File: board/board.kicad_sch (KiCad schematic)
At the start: 17 parts, among them J1 Conn_01x10_Pin, J2 Conn_01x10, U1 nPM1300-CAXX

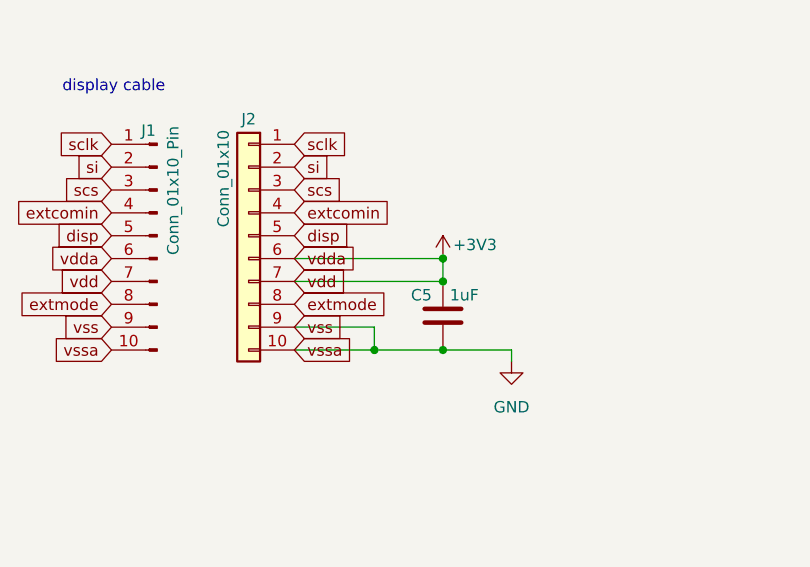
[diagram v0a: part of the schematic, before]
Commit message: board: sch display add extmode and extcomin
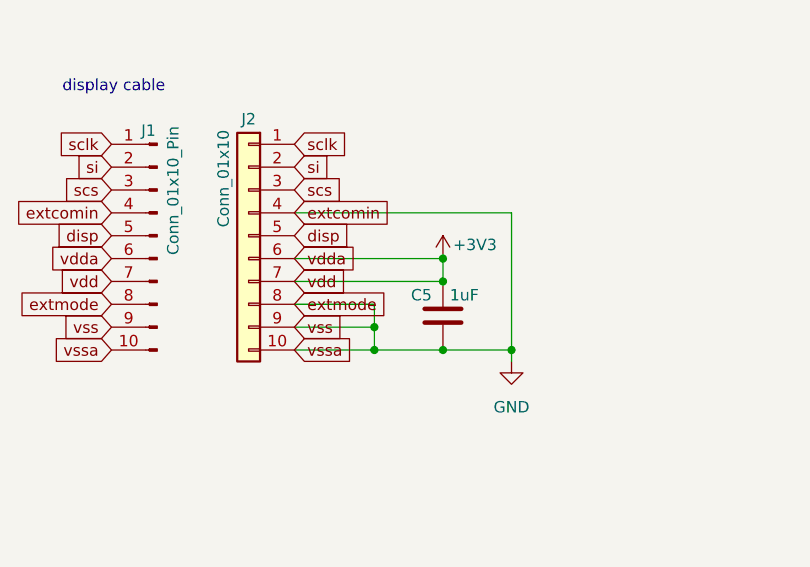
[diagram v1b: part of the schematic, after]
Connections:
- net extcomin is gone; now on net GND: J1.4 (Pin_4), J2.4 (Pin_4)
- net extmode is gone; now on net GND: J1.8 (Pin_8), J2.8 (Pin_8)
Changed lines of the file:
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@@
+	)
+	(junction
+		(at 54.61 48.26)
+		(diameter 0)
+		(color 0 0 0 0)
 	)
 	(junction
@@
 	)
 	(junction
+		(at 69.85 50.8)
+		(diameter 0)
+		(color 0 0 0 0)
+	)
+	(junction
 		(at 261.62 41.91)
 		(diameter 0)
@@
 	(wire
 		(pts
+			(xy 45.72 45.72) (xy 54.61 45.72)
+		)
+		(stroke
+			(width 0)
+			(type default)
+		)
+	)
+	(wire
+		(pts
 			(xy 254 60.96) (xy 252.73 60.96)
 		)
@@
 	(wire
 		(pts
+			(xy 54.61 45.72) (xy 54.61 48.26)
+		)
+		(stroke
+			(width 0)
+			(type default)
+		)
+	)
+	(wire
+		(pts
 			(xy 215.9 20.32) (xy 218.44 20.32)
 		)
@@
 	(wire
 		(pts
+			(xy 69.85 35.56) (xy 69.85 50.8)
+		)
+		(stroke
+			(width 0)
+			(type default)
+		)
+	)
+	(wire
+		(pts
 			(xy 215.9 102.87) (xy 215.9 104.14)
 		)
@@
 		)
 		(stroke
+			(width 0)
+			(type default)
+		)
+	)
+	(wire
+		(pts
+			(xy 45.72 35.56) (xy 69.85 35.56)
+		)
+		(stroke

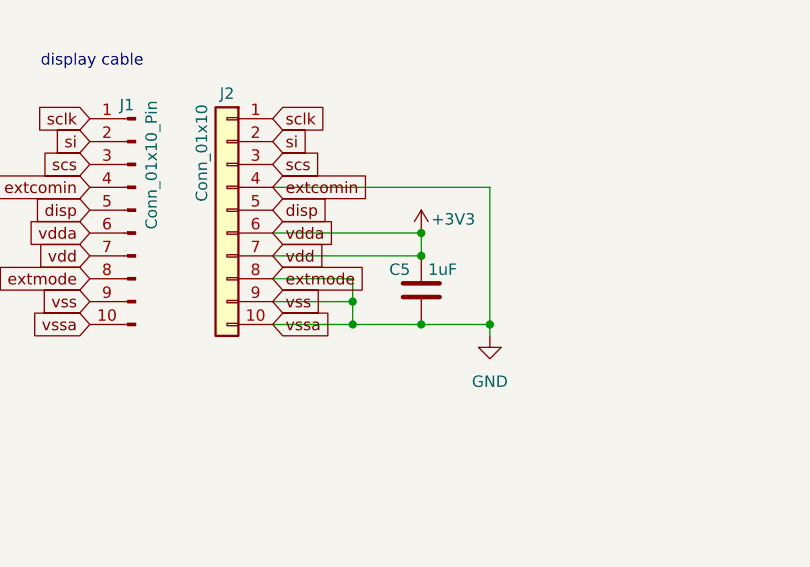
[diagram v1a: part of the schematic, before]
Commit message: board: sch display add disp signal
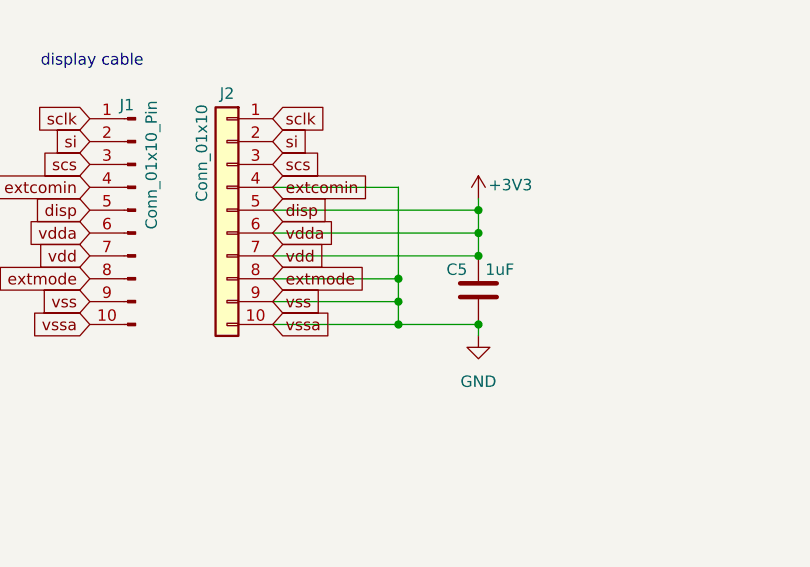
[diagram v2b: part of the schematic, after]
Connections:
- net disp is gone; now on net +3V3: J1.5 (Pin_5), J2.5 (Pin_5)
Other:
- moved on the sheet: C5
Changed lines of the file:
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@@
-	)
-	(junction
-		(at 54.61 48.26)
-		(diameter 0)
-		(color 0 0 0 0)
 	)
 	(junction
@@
 	)
 	(junction
-		(at 62.23 50.8)
+		(at 68.58 50.8)
 		(diameter 0)
 		(color 0 0 0 0)
@@
 	)
 	(junction
-		(at 62.23 40.64)
+		(at 68.58 38.1)
 		(diameter 0)
 		(color 0 0 0 0)
 	)
 	(junction
-		(at 54.61 50.8)
+		(at 59.69 50.8)
+		(diameter 0)
+		(color 0 0 0 0)
+	)
+	(junction
+		(at 68.58 40.64)
 		(diameter 0)
 		(color 0 0 0 0)
@@
 	)
 	(junction
-		(at 69.85 50.8)
+		(at 59.69 45.72)
+		(diameter 0)
+		(color 0 0 0 0)
+	)
+	(junction
+		(at 59.69 48.26)
 		(diameter 0)
 		(color 0 0 0 0)
@@
 	)
 	(junction
-		(at 62.23 43.18)
+		(at 68.58 43.18)
 		(diameter 0)
 		(color 0 0 0 0)
@@
 	(wire
 		(pts
-			(xy 54.61 48.26) (xy 54.61 50.8)
+			(xy 59.69 48.26) (xy 59.69 50.8)
 		)
 		(stroke
@@
 	(wire
 		(pts
-			(xy 54.61 50.8) (xy 62.23 50.8)
-		)
-		(stroke
-			(width 0)
-			(type default)
-		)
-	)
-	(wire
-		(pts
-			(xy 45.72 48.26) (xy 54.61 48.26)
-		)
-		(stroke
-			(width 0)
-			(type default)
-		)
-	)
-	(wire
-		(pts
-			(xy 62.23 40.64) (xy 62.23 43.18)
-		)
-		(stroke
-			(width 0)
-			(type default)
-		)
-	)
-	(wire
-		(pts
-			(xy 45.72 45.72) (xy 54.61 45.72)
+			(xy 45.72 48.26) (xy 59.69 48.26)
+		)
+		(stroke
+			(width 0)
+			(type default)
+		)
+	)
+	(wire
+		(pts
+			(xy 68.58 40.64) (xy 68.58 43.18)
+		)
+		(stroke
+			(width 0)
+			(type default)
+		)
+	)
+	(wire
+		(pts
+			(xy 45.72 45.72) (xy 59.69 45.72)
 		)
 		(stroke
@@
 	(wire
 		(pts
+			(xy 59.69 50.8) (xy 68.58 50.8)
+		)
+		(stroke
+			(width 0)
+			(type default)
+		)
+	)
+	(wire
+		(pts
 			(xy 252.73 57.15) (xy 266.7 57.15)
 		)
@@
 	(wire
 		(pts
-			(xy 45.72 43.18) (xy 62.23 43.18)
-		)
-		(stroke
-			(width 0)
-			(type default)
-		)
-	)
-	(wire
-		(pts
-			(xy 54.61 45.72) (xy 54.61 48.26)
+			(xy 59.69 45.72) (xy 59.69 48.26)
 		)
 		(stroke
@@
 	(wire
 		(pts
-			(xy 69.85 52.07) (xy 69.85 50.8)
-		)
-		(stroke
-			(width 0)
-			(type default)
-		)
-	)
-	(wire
-		(pts
-			(xy 69.85 35.56) (xy 69.85 50.8)
+			(xy 68.58 52.07) (xy 68.58 50.8)
+		)
+		(stroke
+			(width 0)
+			(type default)
+		)
+	)
+	(wire
+		(pts
+			(xy 59.69 35.56) (xy 59.69 45.72)
 		)
 		(stroke
@@
 	(wire
 		(pts
+			(xy 45.72 38.1) (xy 68.58 38.1)
+		)
+		(stroke
+			(width 0)
+			(type default)
+		)
+	)
+	(wire
+		(pts
+			(xy 45.72 43.18) (xy 68.58 43.18)
+		)
+		(stroke
+			(width 0)
+			(type default)
+		)
+	)
+	(wire
+		(pts
 			(xy 173.99 74.93) (xy 180.34 74.93)
 		)
@@
 	(wire
 		(pts
-			(xy 45.72 40.64) (xy 62.23 40.64)
-		)
-		(stroke
-			(width 0)
-			(type default)
-		)
-	)
-	(wire
-		(pts
 			(xy 251.46 62.23) (xy 261.62 62.23)
 		)
@@
 	(wire
 		(pts
-			(xy 45.72 35.56) (xy 69.85 35.56)
-		)
-		(stroke
-			(width 0)
-			(type default)
-		)
-	)
-	(wire
-		(pts
-			(xy 69.85 50.8) (xy 62.23 50.8)
+			(xy 45.72 40.64) (xy 68.58 40.64)
 		)
 		(stroke
@@
 	(wire
 		(pts
+			(xy 68.58 38.1) (xy 68.58 40.64)
+		)
+		(stroke
+			(width 0)
+			(type default)
+		)
+	)
+	(wire
+		(pts
 			(xy 266.7 55.88) (xy 266.7 57.15)
 		)
@@
 	(wire
 		(pts
-			(xy 45.72 50.8) (xy 54.61 50.8)
+			(xy 45.72 50.8) (xy 59.69 50.8)
 		)
 		(stroke
@@
 	(wire
 		(pts
+			(xy 68.58 36.83) (xy 68.58 38.1)
+		)
+		(stroke
+			(width 0)
+			(type default)
+		)
+	)
+	(wire
+		(pts
 			(xy 252.73 41.91) (xy 255.27 41.91)
+		)
+		(stroke
+			(width 0)
+			(type default)
+		)
+	)
+	(wire
+		(pts
+			(xy 45.72 35.56) (xy 59.69 35.56)
 		)
 		(stroke
@@
 	(symbol
 		(lib_id "power:GND")
-		(at 69.85 52.07 0)
+		(at 68.58 52.07 0)
 		(unit 1)
 		(exclude_from_sim no)
@@
 		(fields_autoplaced yes)
 		(property "Reference" "#PWR012"
-			(at 69.85 58.42 0)
+			(at 68.58 58.42 0)
 			(effects
 				(font
@@
 		)
 		(property "Value" "GND"
-			(at 69.85 57.15 0)
+			(at 68.58 57.15 0)
 			(effects
 				(font
@@
 		)
 		(property "Footprint" ""
-			(at 69.85 52.07 0)
+			(at 68.58 52.07 0)
 			(effects
 				(font
@@
 		)
 		(property "Datasheet" ""
-			(at 69.85 52.07 0)
+			(at 68.58 52.07 0)
 			(effects
 				(font
@@
 		)
 		(property "Description" "Power symbol creates a global label with name \"GND\" , ground"
-			(at 69.85 52.07 0)
+			(at 68.58 52.07 0)
 			(effects
 				(font
@@
 	(symbol
 		(lib_id "power:+3V3")
-		(at 62.23 40.64 0)
+		(at 68.58 36.83 0)
 		(unit 1)
 		(exclude_from_sim no)
@@
 		(dnp no)
 		(property "Reference" "#PWR013"
-			(at 62.23 44.45 0)
+			(at 68.58 40.64 0)
 			(effects
 				(font
@@
 		)
 		(property "Value" "+3V3"
-			(at 65.786 39.116 0)
+			(at 72.136 35.306 0)
 			(effects
 				(font
@@
 		)
 		(property "Footprint" ""
-			(at 62.23 40.64 0)
+			(at 68.58 36.83 0)
 			(effects
 				(font
@@
 		)
 		(property "Datasheet" ""
-			(at 62.23 40.64 0)
+			(at 68.58 36.83 0)
 			(effects
 				(font
@@
 		)
 		(property "Description" "Power symbol creates a global label with name \"+3V3\""
-			(at 62.23 40.64 0)
+			(at 68.58 36.83 0)
 			(effects
 				(font
@@
 	(symbol
 		(lib_id "Device:C")
-		(at 62.23 46.99 0)
+		(at 68.58 46.99 0)
 		(unit 1)
 		(exclude_from_sim no)
@@
 		(dnp no)
 		(property "Reference" "C5"
-			(at 58.674 44.704 0)
+			(at 65.024 44.704 0)
 			(effects
 				(font
@@
 		)
 		(property "Value" "1uF"
-			(at 62.992 44.704 0)
+			(at 69.342 44.704 0)
 			(effects
 				(font
@@
 		)
 		(property "Footprint" ""
-			(at 63.1952 50.8 0)
+			(at 69.5452 50.8 0)
 			(effects
 				(font
@@
 		)
 		(property "Datasheet" "~"
-			(at 62.23 46.99 0)
+			(at 68.58 46.99 0)
 			(effects
 				(font
@@
 		)
 		(property "Description" "Unpolarized capacitor"
-			(at 62.23 46.99 0)
-			(effects
-				(font
+			(at 68.58 46.99 0)
+			(effects
+				(font

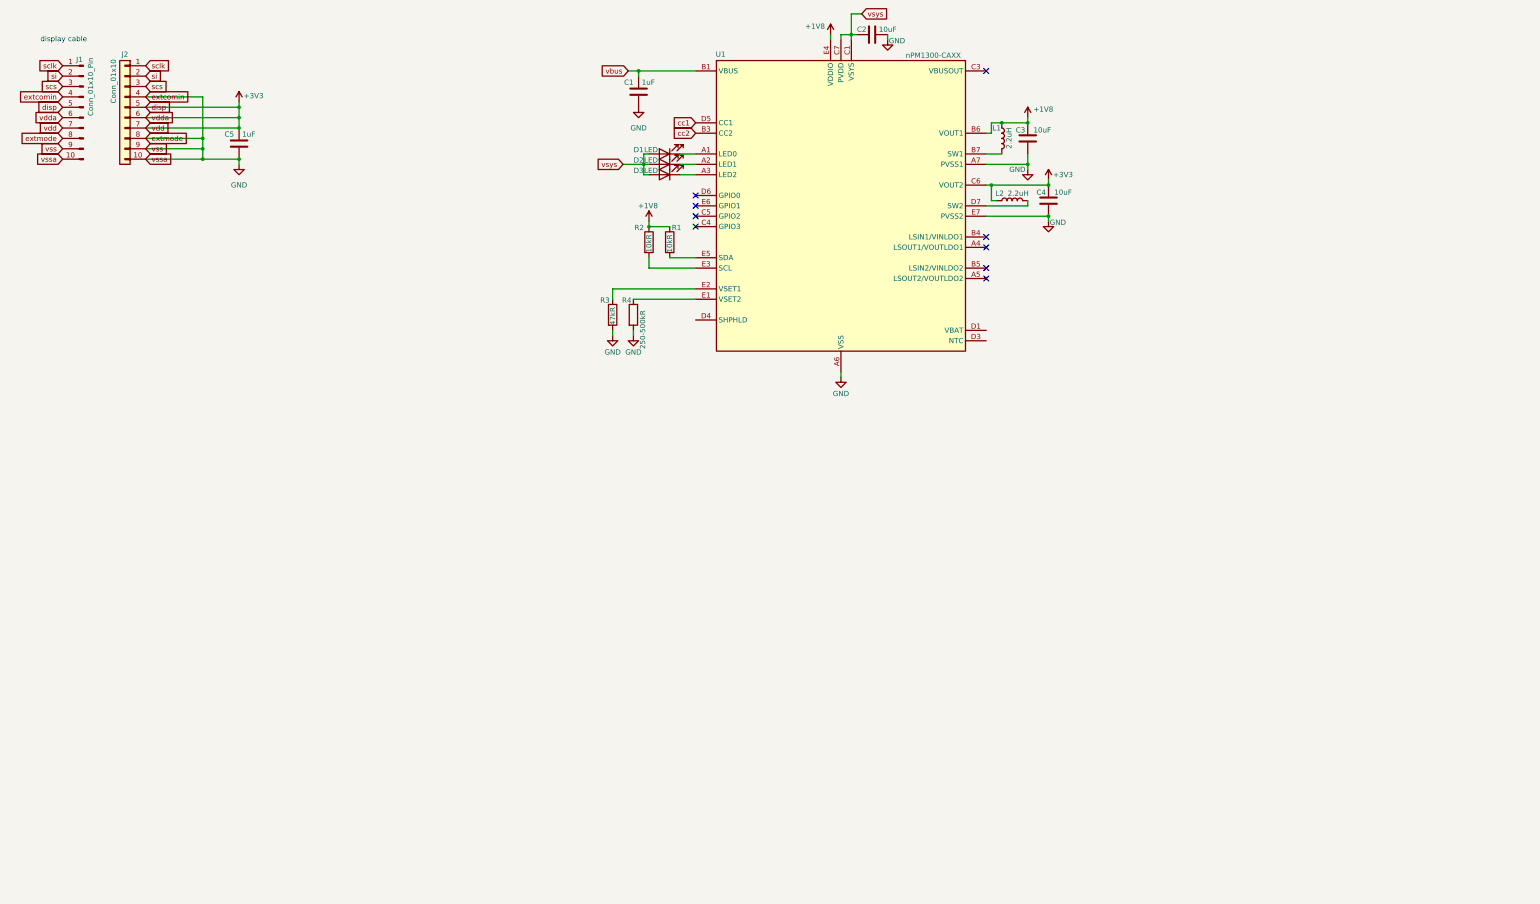
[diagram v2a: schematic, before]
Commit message: board: sch board to board connector
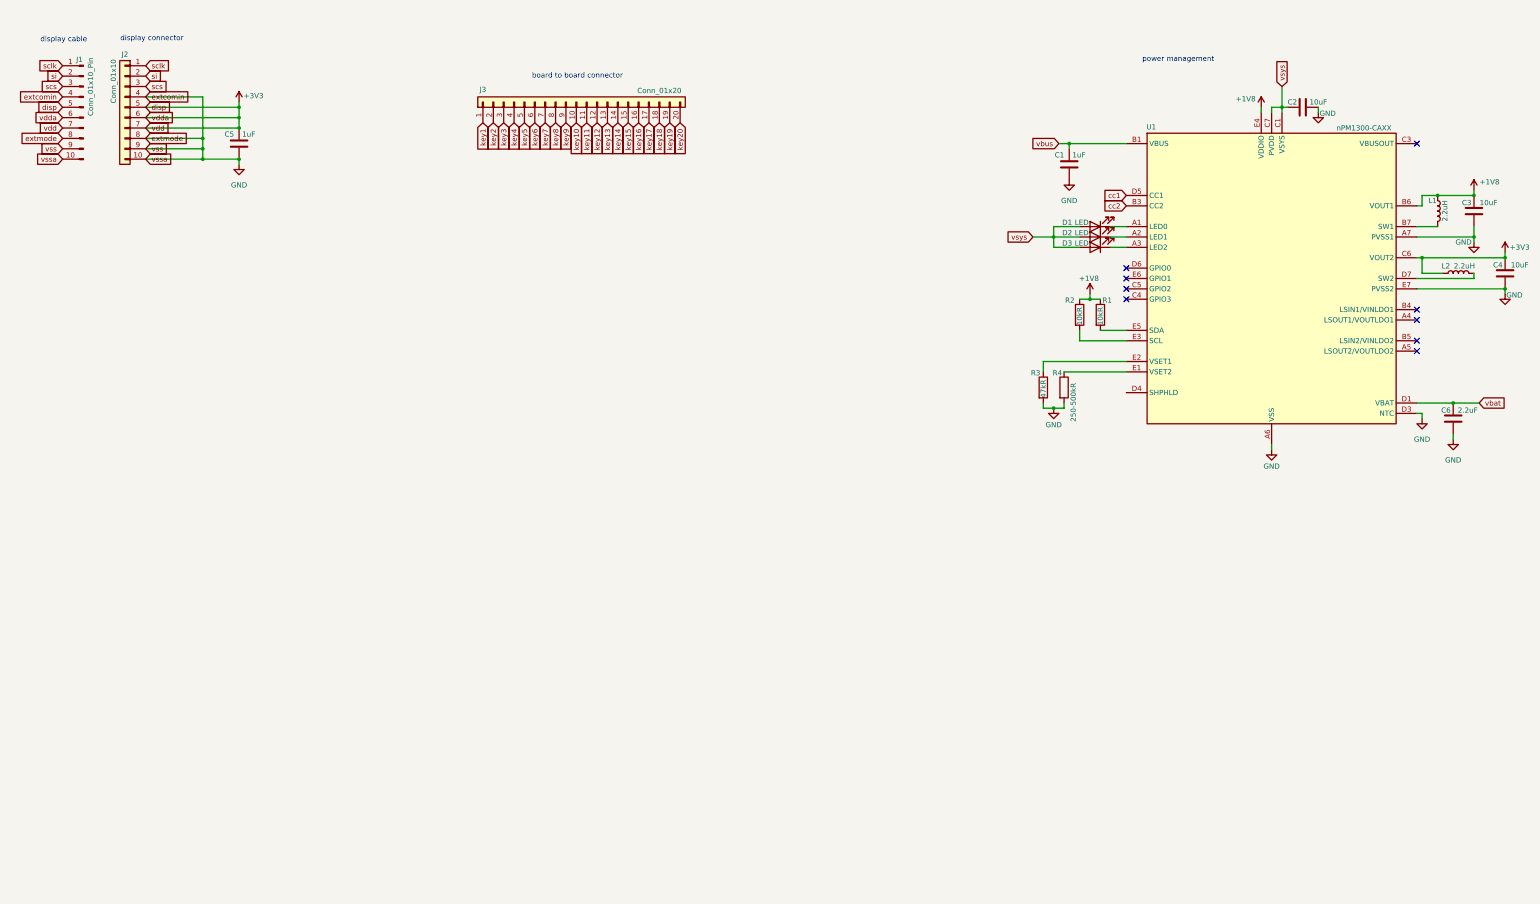
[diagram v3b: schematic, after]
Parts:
- added C6: 2.2uF, symbol Device:C
- added J3: Conn_01x20, symbol Connector_Generic:Conn_01x20
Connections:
- net GND: now also U1.D3 (NTC), C6.2
- net vbat: now reaches U1.D1 (VBAT), U1.D2 (VBAT)
- net vbat: now also C6.1
- new net key1: J3.1 (Pin_1)
- new net key10: J3.10 (Pin_10)
- new net key11: J3.11 (Pin_11)
- new net key12: J3.12 (Pin_12)
- new net key13: J3.13 (Pin_13)
- new net key14: J3.14 (Pin_14)
- new net key15: J3.15 (Pin_15)
- new net key16: J3.16 (Pin_16)
- new net key17: J3.17 (Pin_17)
- new net key18: J3.18 (Pin_18)
- new net key19: J3.19 (Pin_19)
- new net key2: J3.2 (Pin_2)
- new net key20: J3.20 (Pin_20)
- new net key3: J3.3 (Pin_3)
- new net key4: J3.4 (Pin_4)
- new net key5: J3.5 (Pin_5)
- new net key6: J3.6 (Pin_6)
- new net key7: J3.7 (Pin_7)
- new net key8: J3.8 (Pin_8)
- new net key9: J3.9 (Pin_9)
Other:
- note added: "board to board connector"
- note added: "display connector"
- note added: "power management"
- moved on the sheet: C1, C2, C3, C4, D1, D2, D3, L1, L2, R1, R2, R3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

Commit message: board: sch internal usb connector
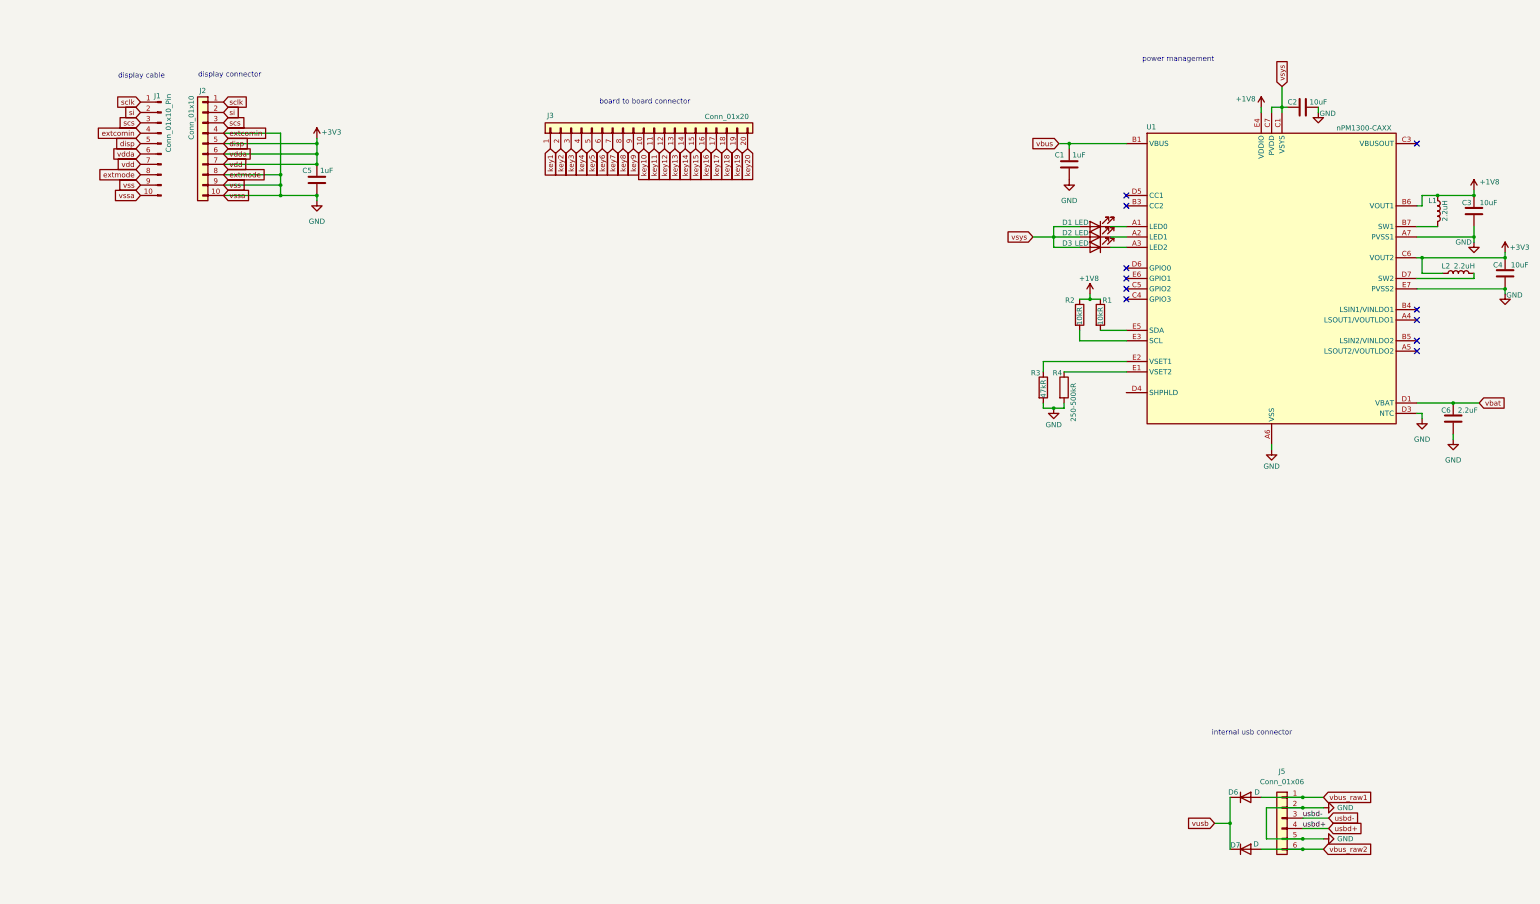
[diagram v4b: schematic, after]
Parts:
- added D6, D7: D, symbol Device:D
- added J5: Conn_01x06, symbol Connector_Generic:Conn_01x06
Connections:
- net GND: now also J5.2 (Pin_2), J5.5 (Pin_5)
- net cc1: no longer names the net of U1.D5 (CC1)
- net cc2: no longer names the net of U1.B3 (CC2)
- new net usbd+: J5.4 (Pin_4)
- new net usbd-: J5.3 (Pin_3)
- new net vbus_raw1: D6.2 (A), J5.1 (Pin_1)
- new net vbus_raw2: D7.2 (A), J5.6 (Pin_6)
- new net vusb: D6.1 (K), D7.1 (K)
- no-connect marks 9 -> 11
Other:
- note added: "internal usb connector"
- moved on the sheet: C5, J1, J2, J3
